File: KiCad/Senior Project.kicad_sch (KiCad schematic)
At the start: 17 parts, among them J1 USB_C_Receptacle_USB2.0_16P, J2 Screw_Terminal_01x02, J3 Screw_Terminal_01x06, J4 Conn_ARM_JTAG_SWD_10, J5 Conn_01x03, SW1 SW_Push, U1 ESP32-S3-WROOM-1

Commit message: Footprints
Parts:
- J5: footprint (none) -> Connector_PinHeader_2.54mm:PinHeader_1x03_P2.54mm_Vertical
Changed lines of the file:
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@@
 			)
 		)
-		(property "Footprint" ""
+		(property "Footprint" "Connector_PinHeader_2.54mm:PinHeader_1x03_P2.54mm_Vertical"
 			(at 254 120.65 0)
 			(effects

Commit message: Routing and placement
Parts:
- U1: footprint PCM_Espressif:ESP32-S3-WROOM-1 -> RF_Module:ESP32-S3-WROOM-1U
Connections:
- net GPS_Reset: now also U1.4 (GPIO4/TOUCH4/ADC1_CH3); no longer U1.7 (GPIO7/TOUCH7/ADC1_CH6)
- net Sense 3: now also U1.7 (GPIO7/TOUCH7/ADC1_CH6); no longer U1.4 (GPIO4/TOUCH4/ADC1_CH3)
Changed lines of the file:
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@@
-		)
-	)
-	(label "Sense 3"
-		(at 196.85 81.28 0)
-		(effects
-			(font
-				(size 1.27 1.27)
-			)
-			(justify left bottom)
 		)
 	)
@@
 		)
 	)
-	(label "GPS_Reset"
-		(at 196.85 88.9 0)
-		(effects
-			(font
-				(size 1.27 1.27)
-			)
-			(justify left bottom)
-		)
-	)
 	(label "MTDI"
 		(at 95.25 76.2 0)
@@
 		)
 	)
+	(label "Sense 3"
+		(at 196.85 88.9 0)
+		(effects
+			(font
+				(size 1.27 1.27)
+			)
+			(justify left bottom)
+		)
+	)
 	(label "RADIO_RST"
 		(at 196.85 106.68 0)
@@
 		)
 	)
+	(label "GPS_Reset"
+		(at 196.85 81.28 0)
+		(effects
+			(font
+				(size 1.27 1.27)
+			)
+			(justify left bottom)
+		)
+	)
 	(label "UOTXD"
 		(at 243.84 118.11 0)
@@
 			)
 		)
-		(property "Footprint" "PCM_Espressif:ESP32-S3-WROOM-1"
+		(property "Footprint" "RF_Module:ESP32-S3-WROOM-1U"
 			(at 151.13 139.7 0)
 			(effects

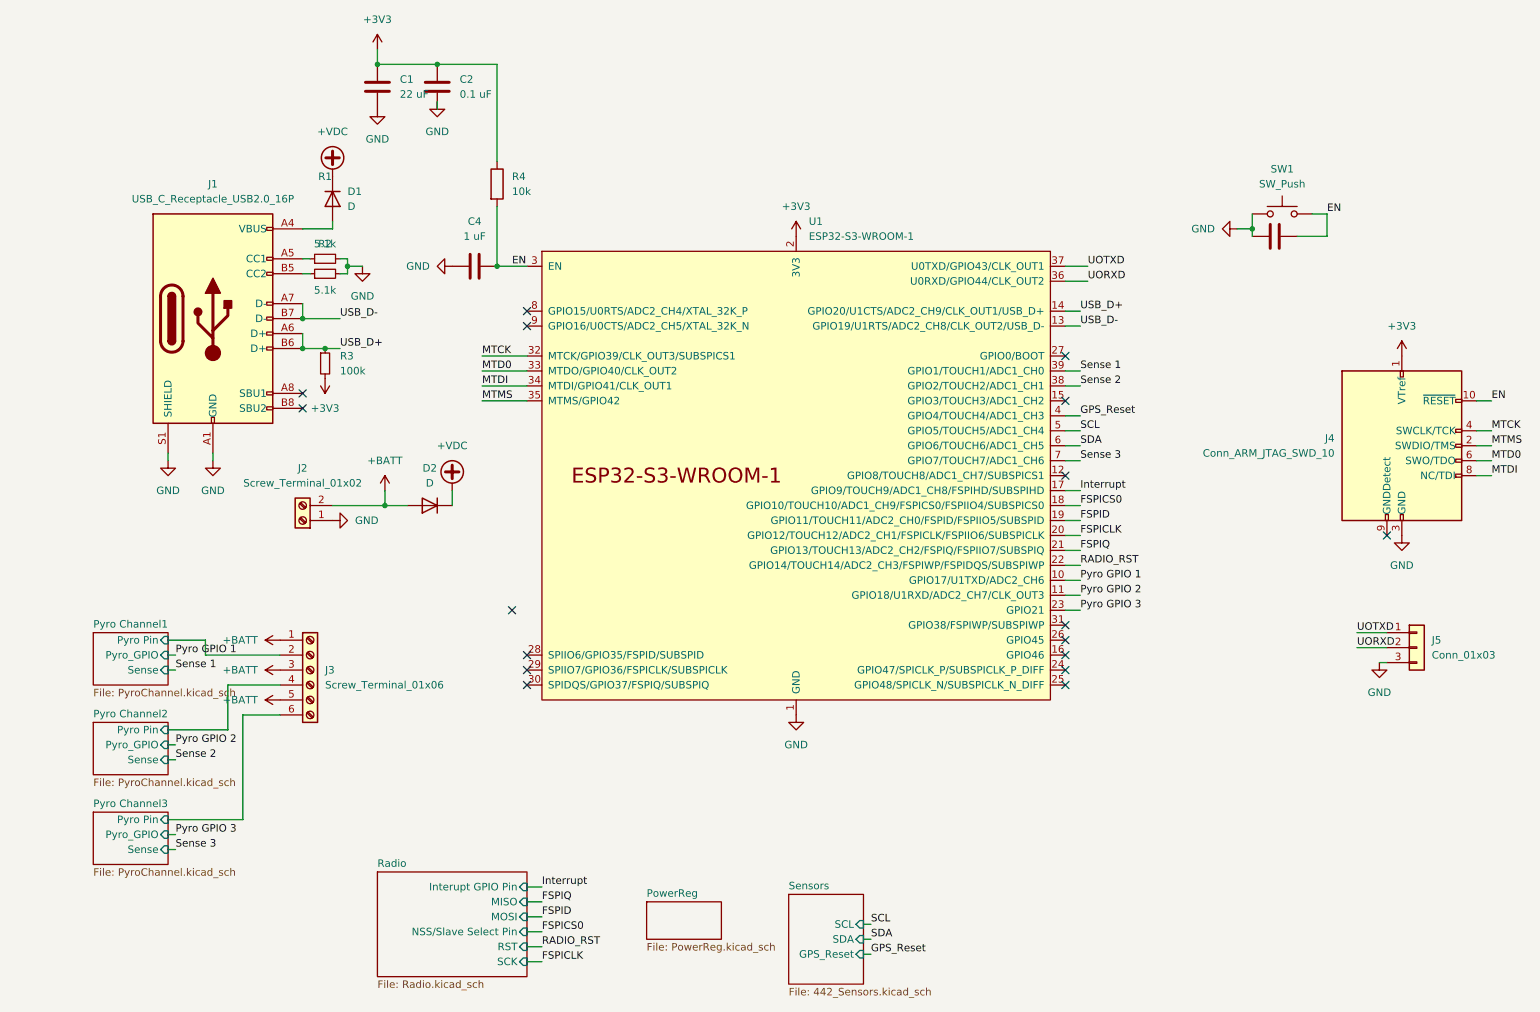
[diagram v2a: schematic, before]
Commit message: DRC issues, only a few signals left to be routed
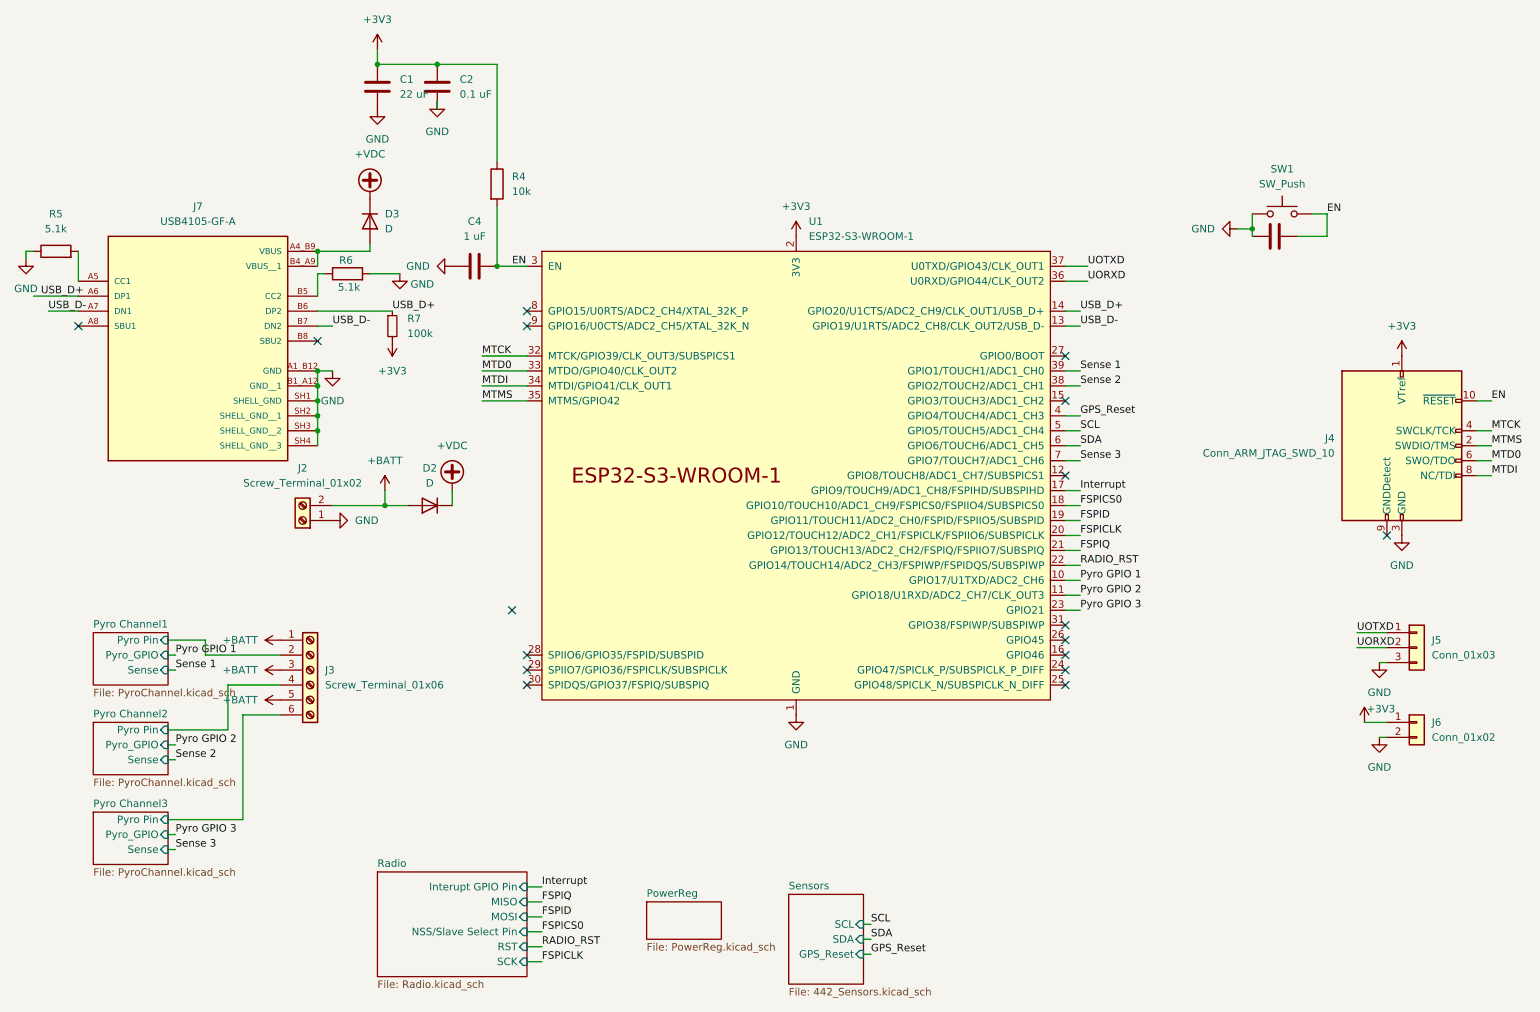
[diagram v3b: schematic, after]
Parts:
- removed D1: D, VS_10BQ015HM3_5BT:CR_SMBDO-214AA_VIS, symbol Device:D
- removed J1: USB_C_Receptacle_USB2.0_16P, USB4105_GF_A (1):GCT_USB4105-GF-A, symbol Connector:USB_C_Receptacle_USB2.0_16P
- removed R1, R2: 5.1k, Resistor_SMD:R_0402_1005Metric, symbol Device:R_Small
- removed R3: 100k, Resistor_SMD:R_0402_1005Metric, symbol Device:R_Small
- added D3: D, VS_10BQ015HM3_5BT:CR_SMBDO-214AA_VIS, symbol Device:D
- added J6: Conn_01x02, Connector_PinHeader_2.54mm:PinHeader_1x02_P2.54mm_Vertical, symbol Connector_Generic:Conn_01x02
- added J7: USB4105-GF-A, USB4105_GF_A (1):GCT_USB4105-GF-A, symbol USB4105-GF-A:USB4105-GF-A
- added R5, R6: 5.1k, Resistor_SMD:R_0402_1005Metric, symbol Device:R
- added R7: 100k, Resistor_SMD:R_0402_1005Metric, symbol Device:R_Small
- J4: footprint (none) -> Connector_PinHeader_2.54mm:PinHeader_1x10_P2.54mm_Vertical
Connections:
- net +3V3: now also J6.1 (Pin_1), R7.2
- net +VDC: now also D3.1 (K)
- net GND: now also J6.2 (Pin_2), J7.A1_B12 (GND), J7.B1_A12 (GND__1), J7.SH1 (SHELL_GND), J7.SH2 (SHELL_GND__1), J7.SH3 (SHELL_GND__2), J7.SH4 (SHELL_GND__3), R5.1, R6.2
- net USB_D+: now also J7.A6 (DP1), J7.B6 (DP2), R7.1
- net USB_D-: now also J7.A7 (DN1), J7.B7 (DN2)
- new net: J7.A5 (CC1), R5.2
- new net: D3.2 (A), J7.A4_B9 (VBUS), J7.B4_A9 (VBUS__1)
- new net: J7.B5 (CC2), R6.1

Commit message: Fixes based on comments, entered design constraints
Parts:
- J4: footprint Connector_PinHeader_2.54mm:PinHeader_1x10_P2.54mm_Vertical -> Connector_PinHeader_1.27mm:PinHeader_2x05_P1.27mm_Vertical
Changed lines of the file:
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@@
 			)
 		)
-		(property "Footprint" "Connector_PinHeader_2.54mm:PinHeader_1x10_P2.54mm_Vertical"
+		(property "Footprint" "Connector_PinHeader_1.27mm:PinHeader_2x05_P1.27mm_Vertical"
 			(at 251.46 86.36 0)
 			(effects

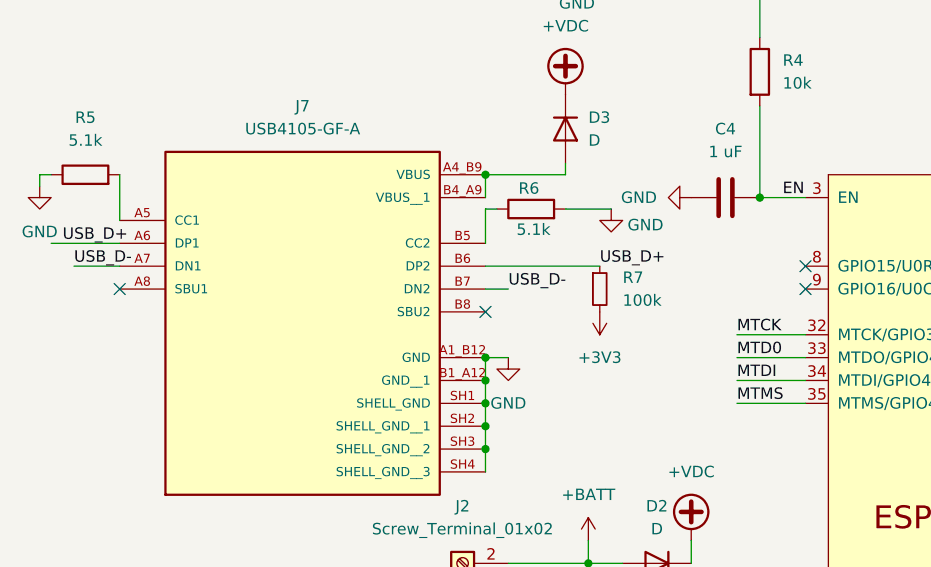
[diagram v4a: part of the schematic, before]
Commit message: Max's feedback taken into account, have to add RF trace
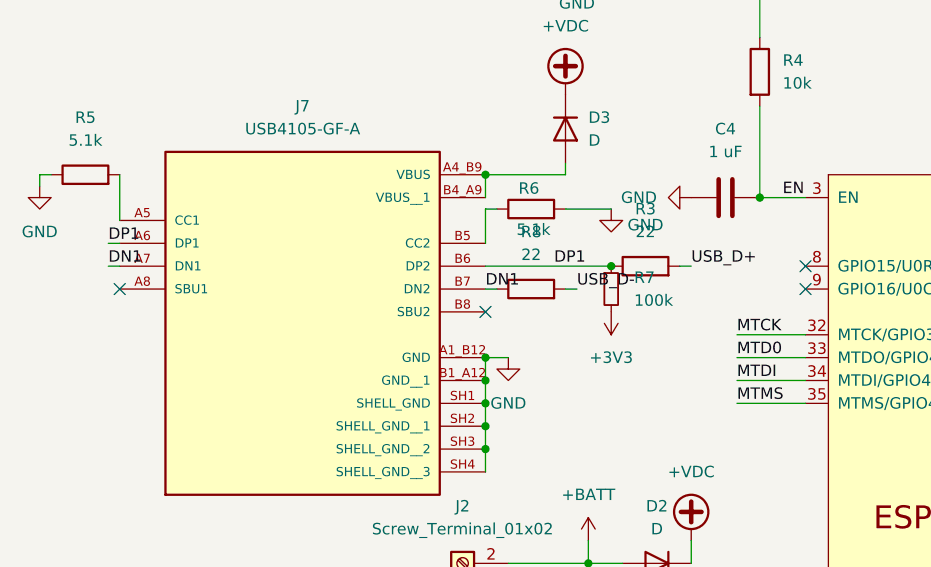
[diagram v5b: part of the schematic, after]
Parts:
- added R3, R8: 22, Resistor_SMD:R_0402_1005Metric, symbol Device:R
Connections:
- net USB_D+: now also R3.2; no longer J7.A6 (DP1), J7.B6 (DP2), R7.1
- net USB_D-: now also R8.2; no longer J7.A7 (DN1), J7.B7 (DN2)
- new net DN1: J7.A7 (DN1), J7.B7 (DN2), R8.1
- new net DP1: J7.A6 (DP1), J7.B6 (DP2), R3.1, R7.1
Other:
- moved on the sheet: R7

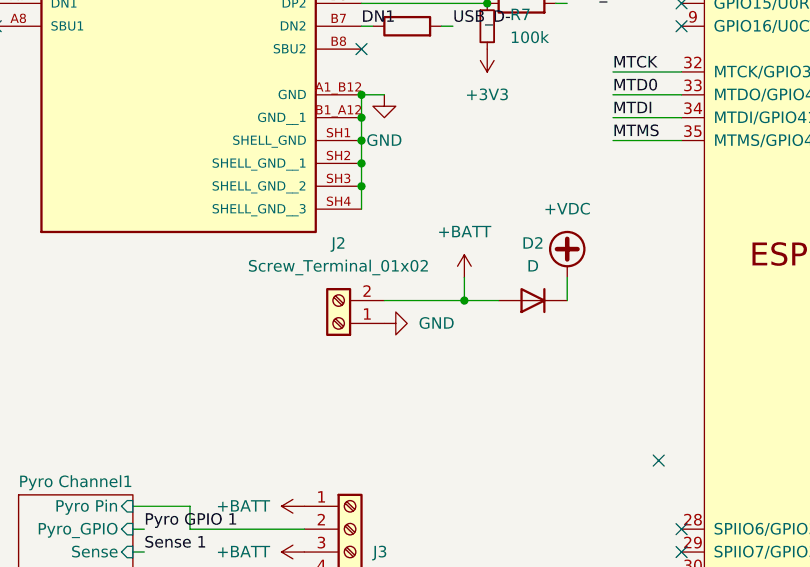
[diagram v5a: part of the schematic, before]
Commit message: Barometer schematic fix, JST connector, and few other fixes
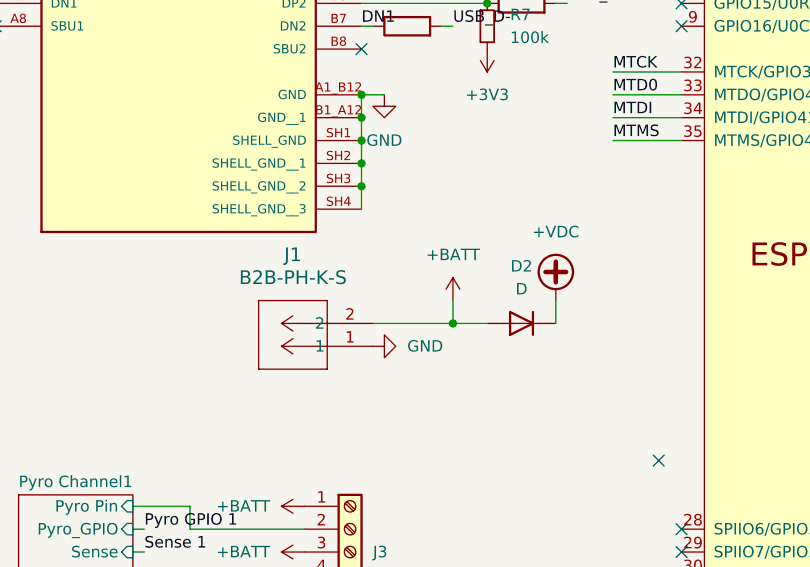
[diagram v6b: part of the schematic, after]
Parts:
- removed J2: Screw_Terminal_01x02, OSTVN02A150:CONN_OSTVN02A150_OST, symbol Connector:Screw_Terminal_01x02
- added J1: B2B-PH-K-S, CONN2_B2B-PH-K-S_JST, symbol JST_Connector:B2B-PH-K-S
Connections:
- net +BATT: now also J1.2
- net GND: now also J1.1
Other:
- moved on the sheet: D2
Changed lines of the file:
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@@
 	)
 	(junction
-		(at 78.74 96.52)
-		(diameter 0)
-		(color 0 0 0 0)
-	)
-	(junction
 		(at 97.79 55.88)
 		(diameter 0)
@@
 	)
 	(junction
+		(at 77.47 99.06)
+		(diameter 0)
+		(color 0 0 0 0)
+	)
+	(junction
 		(at 67.31 73.66)
 		(diameter 0)
@@
 	(wire
 		(pts
-			(xy 69.85 96.52) (xy 78.74 96.52)
-		)
-		(stroke
-			(width 0)
-			(type default)
-		)
-	)
-	(wire
-		(pts
 			(xy 41.91 154.94) (xy 43.18 154.94)
 		)
@@
 	(wire
 		(pts
+			(xy 68.58 99.06) (xy 77.47 99.06)
+		)
+		(stroke
+			(width 0)
+			(type default)
+		)
+	)
+	(wire
+		(pts
 			(xy 77.47 21.59) (xy 87.63 21.59)
 		)
@@
 	(wire
 		(pts
-			(xy 90.17 93.98) (xy 90.17 96.52)
+			(xy 88.9 96.52) (xy 88.9 99.06)
 		)
 		(stroke
@@
 	(wire
 		(pts
-			(xy 78.74 93.98) (xy 78.74 96.52)
+			(xy 77.47 96.52) (xy 77.47 99.06)
 		)
 		(stroke
@@
 	(wire
 		(pts
-			(xy 78.74 96.52) (xy 82.55 96.52)
+			(xy 77.47 99.06) (xy 81.28 99.06)
 		)
 		(stroke
@@
 	(symbol
 		(lib_id "power:GND")
-		(at 69.85 99.06 90)
+		(at 68.58 101.6 90)
 		(unit 1)
 		(exclude_from_sim no)
@@
 		(fields_autoplaced yes)
 		(property "Reference" "#PWR06"
-			(at 76.2 99.06 0)
+			(at 74.93 101.6 0)
 			(effects
 				(font
@@
 		)
 		(property "Value" "GND"
-			(at 73.66 99.0599 90)
+			(at 72.39 101.5999 90)
 			(effects
 				(font
@@
 		)
 		(property "Footprint" ""
-			(at 69.85 99.06 0)
+			(at 68.58 101.6 0)
 			(effects
 				(font
@@
 		)
 		(property "Datasheet" ""
-			(at 69.85 99.06 0)
+			(at 68.58 101.6 0)
 			(effects
 				(font
@@
 		)
 		(property "Description" "Power symbol creates a global label with name \"GND\" , ground"
-			(at 69.85 99.06 0)
+			(at 68.58 101.6 0)
 			(effects
 				(font
@@
 	(symbol
 		(lib_id "power:+VDC")
-		(at 90.17 93.98 0)
+		(at 88.9 96.52 0)
 		(unit 1)
 		(exclude_from_sim no)
@@
 		(fields_autoplaced yes)
 		(property "Reference" "#PWR039"
-			(at 90.17 96.52 0)
+			(at 88.9 99.06 0)
 			(effects
 				(font
@@
 		)
 		(property "Value" "+VDC"
-			(at 90.17 86.36 0)
+			(at 88.9 88.9 0)
 			(effects
 				(font
@@
 		)
 		(property "Footprint" ""
-			(at 90.17 93.98 0)
+			(at 88.9 96.52 0)
 			(effects
 				(font
@@
 		)
 		(property "Datasheet" ""
-			(at 90.17 93.98 0)
+			(at 88.9 96.52 0)
 			(effects
 				(font
@@
 		)
 		(property "Description" "Power symbol creates a global label with name \"+VDC\""
-			(at 90.17 93.98 0)
+			(at 88.9 96.52 0)
 			(effects
 				(font
@@
 	)
 	(symbol
-		(lib_id "Connector:Screw_Terminal_01x02")
-		(at 64.77 99.06 180)
+		(lib_id "Device:D")
+		(at 85.09 99.06 180)
 		(unit 1)
 		(exclude_from_sim no)
@@
 		(dnp no)
 		(fields_autoplaced yes)
-		(property "Reference" "J2"
-			(at 64.77 90.17 0)
+		(property "Reference" "D2"
+			(at 85.09 92.71 0)
 			(effects
 				(font
@@
 			)
 		)
-		(property "Value" "Screw_Terminal_01x02"
-			(at 64.77 92.71 0)
+		(property "Value" "D"
+			(at 85.09 95.25 0)
 			(effects
 				(font
@@
 			)
 		)
-		(property "Footprint" "OSTVN02A150:CONN_OSTVN02A150_OST"
-			(at 64.77 99.06 0)
+		(property "Footprint" "VS_10BQ015HM3_5BT:CR_SMBDO-214AA_VIS"
+			(at 85.09 99.06 0)
 			(effects
 				(font
@@
 		)
 		(property "Datasheet" "~"
-			(at 64.77 99.06 0)
+			(at 85.09 99.06 0)
 			(effects
 				(font
@@
 			)
 		)
-		(property "Description" "Generic screw terminal, single row, 01x02, script generated (kicad-library-utils/schlib/autogen/connector/)"
-			(at 64.77 99.06 0)
+		(property "Description" "Diode"
+			(at 85.09 99.06 0)
+			(effects
+				(font
+					(size 1.27 1.27)
+				)
+				(hide yes)
+			)
+		)
+		(property "Sim.Device" "D"
+			(at 85.09 99.06 0)
+			(effects
+				(font
+					(size 1.27 1.27)
+				)
+				(hide yes)
+			)
+		)
+		(property "Sim.Pins" "1=K 2=A"
+			(at 85.09 99.06 0)
 			(effects
 				(font
@@
 		)
 		(instances
-			(project ""
+			(project "Senior Project"
 				(path "/16f8cce7-467e-4342-b55a-00af81cd6f69"
-					(reference "J2")
+					(reference "D2")
 					(unit 1)
 				)
@@
 	)
 	(symbol
-		(lib_id "Device:D")
-		(at 86.36 96.52 180)
+		(lib_id "power:+BATT")
+		(at 77.47 96.52 0)
 		(unit 1)
 		(exclude_from_sim no)
@@
 		(dnp no)
 		(fields_autoplaced yes)
-		(property "Reference" "D2"
-			(at 86.36 90.17 0)
-			(effects
-				(font
-					(size 1.27 1.27)
-				)
-			)
-		)
-		(property "Value" "D"
-			(at 86.36 92.71 0)
-			(effects
-				(font
-					(size 1.27 1.27)
-				)
-			)
-		)
-		(property "Footprint" "VS_10BQ015HM3_5BT:CR_SMBDO-214AA_VIS"
-			(at 86.36 96.52 0)
+		(property "Reference" "#PWR05"
+			(at 77.47 100.33 0)
 			(effects
 				(font
@@
 			)
 		)
-		(property "Datasheet" "~"
-			(at 86.36 96.52 0)
+		(property "Value" "+BATT"
+			(at 77.47 91.44 0)
 			(effects
 				(font
 					(size 1.27 1.27)
 				)
-				(hide yes)
 			)
 		)
-		(property "Description" "Diode"
-			(at 86.36 96.52 0)
+		(property "Footprint" ""
+			(at 77.47 96.52 0)
 			(effects
 				(font
@@
 			)
 		)
-		(property "Sim.Device" "D"
-			(at 86.36 96.52 0)
+		(property "Datasheet" ""
+			(at 77.47 96.52 0)
 			(effects
 				(font
@@
 			)
 		)
-		(property "Sim.Pins" "1=K 2=A"
-			(at 86.36 96.52 0)
+		(property "Description" "Power symbol creates a global label with name \"+BATT\""
+			(at 77.47 96.52 0)
 			(effects
 				(font
@@
 			)
 		)
-		(pin "2"
-		)
 		(pin "1"
 		)
 		(instances
-			(project "Senior Project"
+			(project ""
 				(path "/16f8cce7-467e-4342-b55a-00af81cd6f69"
-					(reference "D2")
+					(reference "#PWR05")
 					(unit 1)
 				)
@@
 	)
 	(symbol
-		(lib_id "power:+BATT")
-		(at 78.74 93.98 0)
+		(lib_id "JST_Connector:B2B-PH-K-S")
+		(at 68.58 101.6 180)
 		(unit 1)
 		(exclude_from_sim no)
@@
 		(dnp no)
 		(fields_autoplaced yes)
-		(property "Reference" "#PWR05"
-			(at 78.74 97.79 0)
+		(property "Reference" "J1"
+			(at 59.69 91.44 0)
 			(effects
 				(font
-					(size 1.27 1.27)
+					(size 1.524 1.524)
 				)
-				(hide yes)
 			)
 		)
-		(property "Value" "+BATT"
-			(at 78.74 88.9 0)
+		(property "Value" "B2B-PH-K-S"
+			(at 59.69 93.98 0)
 			(effects
 				(font
-					(size 1.27 1.27)
+					(size 1.524 1.524)
 				)
 			)
 		)
-		(property "Footprint" ""
-			(at 78.74 93.98 0)
+		(property "Footprint" "CONN2_B2B-PH-K-S_JST"
+			(at 68.58 101.6 0)
 			(effects
 				(font
 					(size 1.27 1.27)
+					(italic yes)
 				)
 				(hide yes)
 			)
 		)
-		(property "Datasheet" ""
-			(at 78.74 93.98 0)
+		(property "Datasheet" "B2B-PH-K-S"
+			(at 68.58 101.6 0)
 			(effects
 				(font
 					(size 1.27 1.27)
+					(italic yes)
 				)
 				(hide yes)
 			)
 		)
-		(property "Description" "Power symbol creates a global label with name \"+BATT\""
-			(at 78.74 93.98 0)
+		(property "Description" ""
+			(at 68.58 101.6 0)
 			(effects
 				(font
@@
 			)
 		)
+		(pin "2"
+		)
 		(pin "1"
 		)
@@
 			(project ""
 				(path "/16f8cce7-467e-4342-b55a-00af81cd6f69"
-					(reference "#PWR05")
+					(reference "J1")
 					(unit 1)
 				)
